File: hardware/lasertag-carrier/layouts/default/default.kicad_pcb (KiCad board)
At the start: 2 copper layers, 100 x 80 mm, 39 parts, among them J0 Power in 2P, J1 S3-Matrix L, J12 Ext button, J13 Touch hdr, J14 Activity LED, J2 S3-Matrix R, J3 MAX98357A, J4 Speaker, J5 microSD, J6 IR RX, J7 IR LED, J8 WS2812 out, J9 OLED I2C, Q1 2N2222A, SW1 SW_PUSH_6mm, SW2 PWR switch

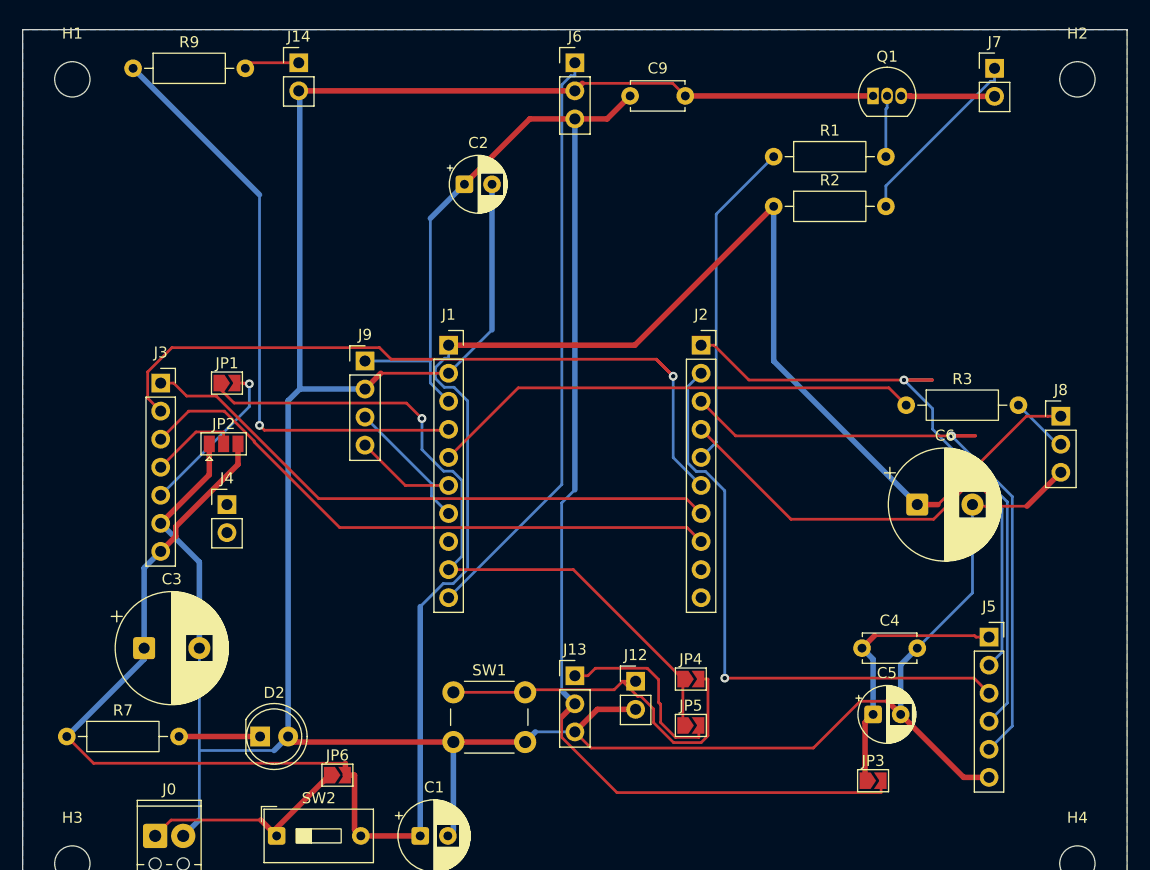
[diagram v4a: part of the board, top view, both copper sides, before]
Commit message: Silk fixes: move edge-clipped refdes inboard, add 5V IN +/- labels
- H1/H2/J6/J14 reference text was clipped by the top board edge; moved below
  each part (silk_edge_clearance 4 -> 0)
- added "5V IN" and +/- polarity marks above J0 (pad 1 = +5V, pad 2 = GND)

Remaining DRC: jumper mask apertures (by design) and 5 track_dangling
warnings that are actually redundant parallel F.Cu/B.Cu segments from the
autorouter -- an independent endpoint-connectivity check confirms both ends
of each are connected (0 unconnected items). Edit > Cleanup Tracks & Vias in
the KiCad GUI removes them if desired.

Co-Authored-By: Claude Opus 4.8 <noreply@anthropic.com>
Claude-Session: https://claude.ai/code/session_01TutNLcDSScdeeVSbjpyg8j
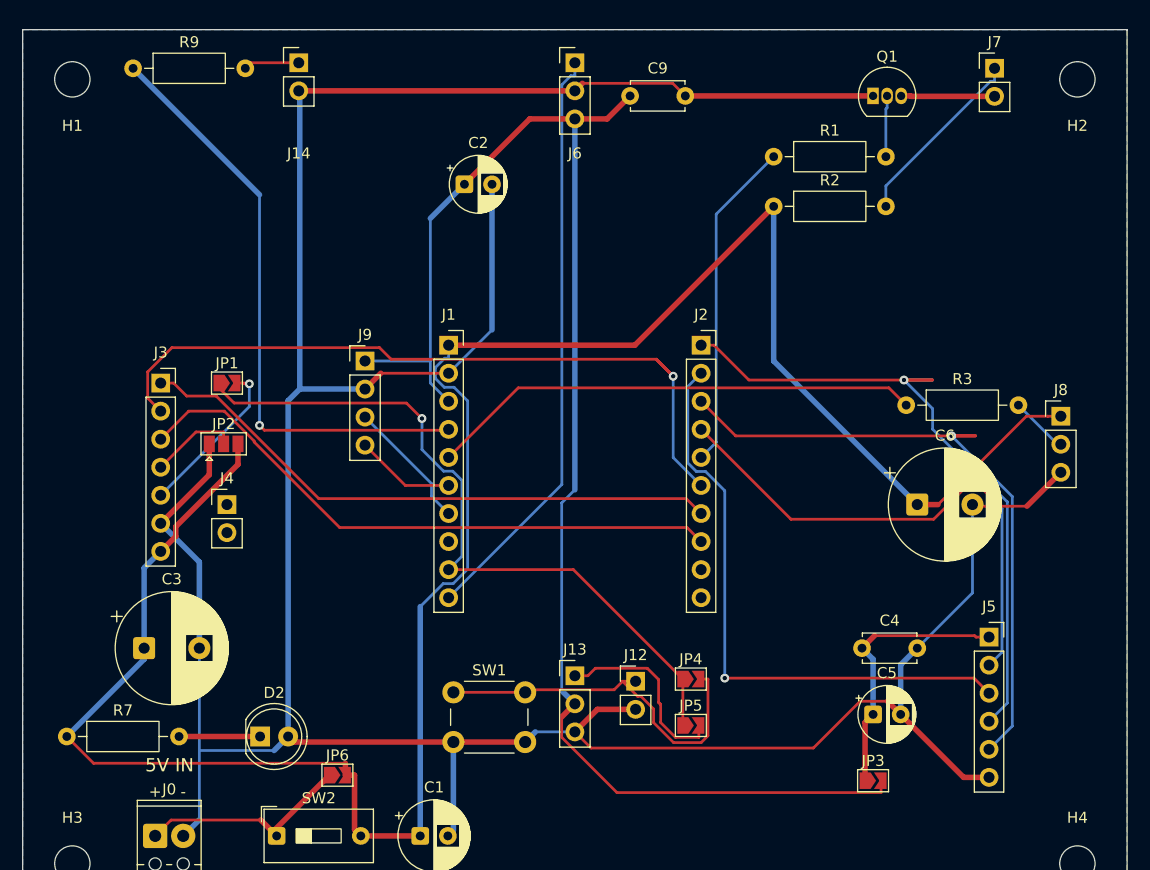
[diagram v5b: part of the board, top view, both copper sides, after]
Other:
- board text added: "+"
- board text added: "-"
- board text added: "5V IN"
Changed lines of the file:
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@@
 		(tags "mountinghole M3")
 		(property "Reference" "H1"
-			(at 0 -4.15 0)
+			(at 0 4.2 0)
 			(layer "F.SilkS")
 			(effects
@@
 		(tags "mountinghole M3")
 		(property "Reference" "H2"
-			(at 0 -4.15 0)
+			(at 0 4.2 0)
 			(layer "F.SilkS")
 			(effects
@@
 		(at 150 63)
 		(property "Reference" "J6"
-			(at 0 -2.38 0)
+			(at 0 8.2 0)
 			(layer "F.SilkS")
 			(effects
@@
 		(at 125 63)
 		(property "Reference" "J14"
-			(at 0 -2.38 0)
+			(at 0 8.2 0)
 			(layer "F.SilkS")
 			(effects
@@
 		(layer "Edge.Cuts")
 	)
+	(gr_text "+"
+		(at 112 129 0)
+		(layer "F.SilkS")
+		(effects
+			(font
+				(size 1 1)
+				(thickness 0.15)
+			)
+		)
+	)
+	(gr_text "-"
+		(at 114.54 129 0)
+		(layer "F.SilkS")
+		(effects
+			(font
+				(size 1 1)
+				(thickness 0.15)
+			)
+		)
+	)
+	(gr_text "5V IN"
+		(at 113.3 126.6 0)
+		(layer "F.SilkS")
+		(effects
+			(font
+				(size 1.2 1.2)
+				(thickness 0.15)
+			)
+		)
+	)
 	(segment

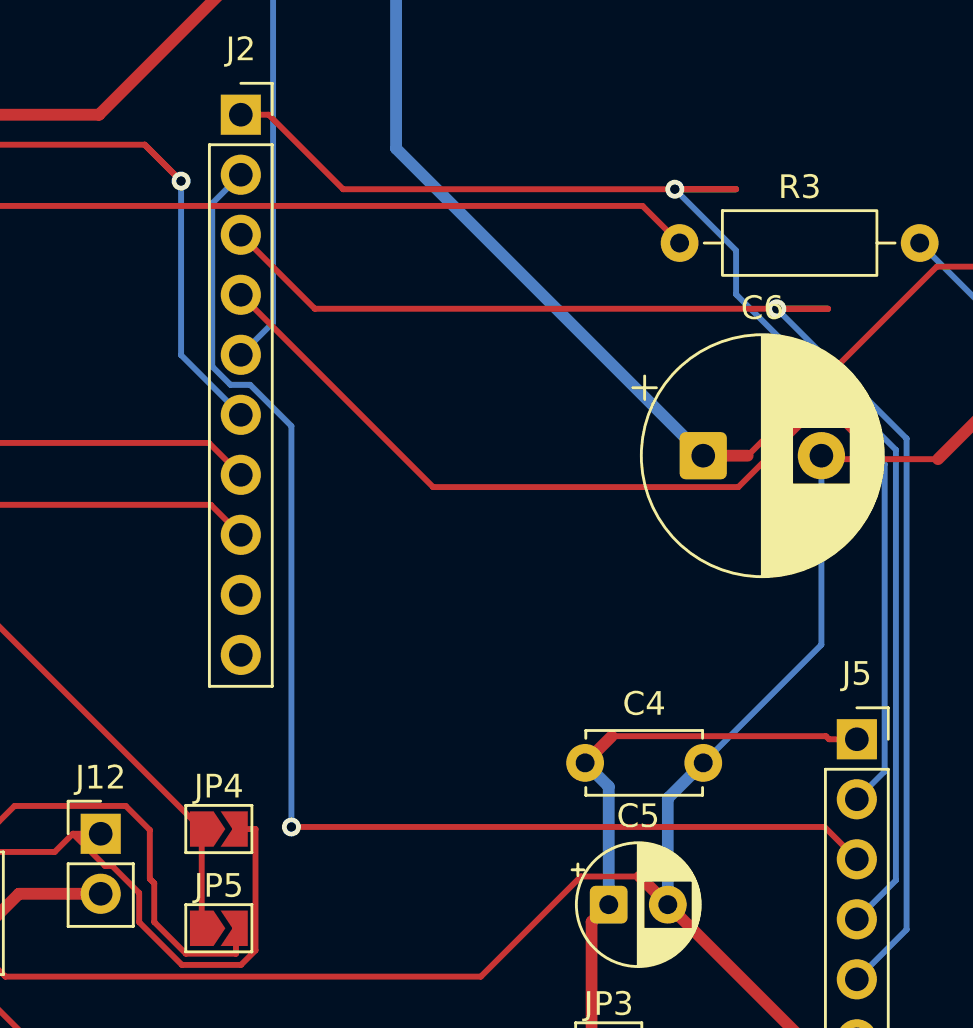
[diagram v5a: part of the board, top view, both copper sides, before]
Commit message: DRC to zero: jumper mask-bridge attr restored, redundant tracks removed
- set allow_soldermask_bridges on all six solder jumpers (JP1-JP6) via
  pcbnew FOOTPRINT.SetAllowSolderMaskBridges(True) -- restores the stock
  KiCad behaviour the atopile footprint patch had stripped; also patched the
  LocalJumper library .kicad_mod files so board and library stay in sync
  (solder_mask_bridge 27 -> 0, lib_footprint_mismatch 0)
- removed 13 redundant autorouter segments: 11 stacked exact duplicates
  (same net + same endpoints, up to 3 copies deep on i2s_bclk) found by
  grouping segments by (net, endpoint-set) and keeping one copy, plus the 2
  remaining parallel loops verified removable by checkpoint + re-DRC
  (track_dangling 5 -> 0); no vias were orphaned

Final DRC: zero violations of any kind, zero unconnected items.

Co-Authored-By: Claude Opus 4.8 <noreply@anthropic.com>
Claude-Session: https://claude.ai/code/session_01TutNLcDSScdeeVSbjpyg8j
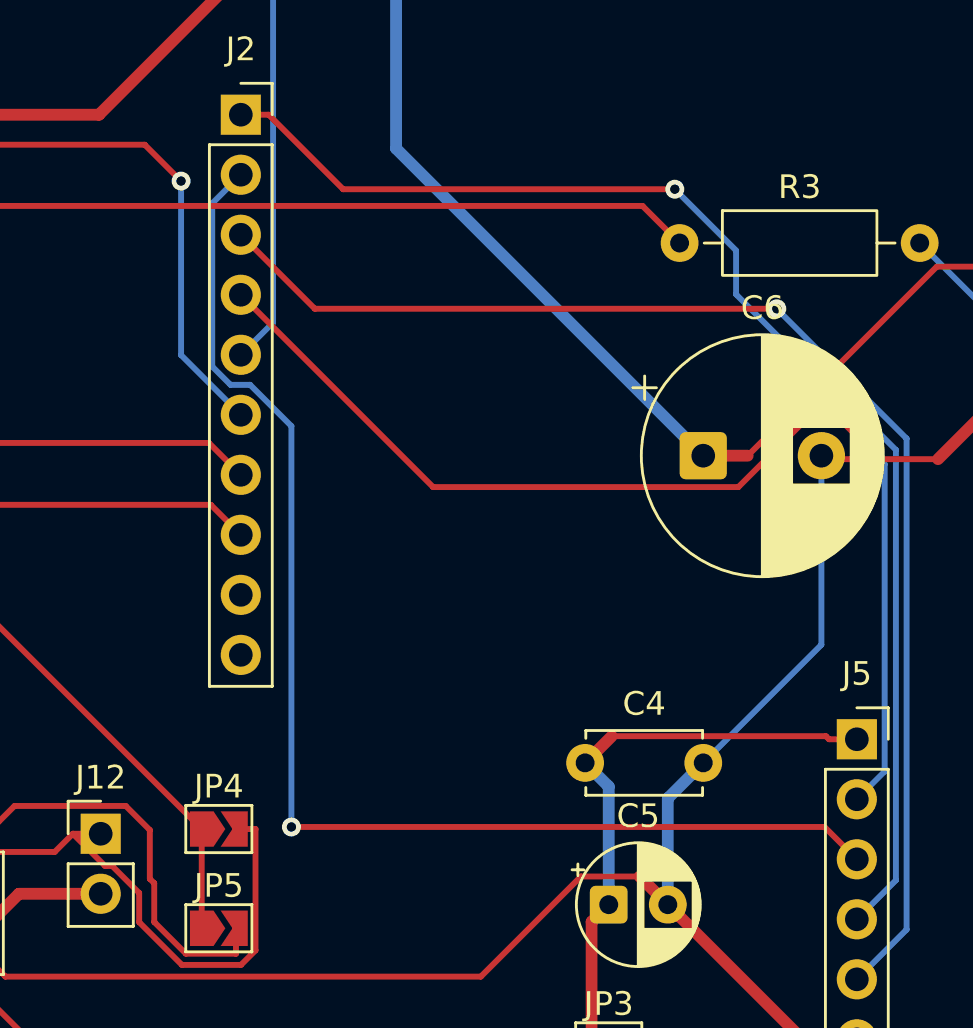
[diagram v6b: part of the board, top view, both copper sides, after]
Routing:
- net sd_sck: track 65.6 -> 55.2 mm
- net i2s_bclk: track 73.2 -> 64.5 mm
- net sd_miso: track 64.2 -> 55.5 mm
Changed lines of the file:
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@@
 			)
 		)
-		(attr exclude_from_pos_files exclude_from_bom)
+		(attr exclude_from_pos_files exclude_from_bom allow_soldermask_bridges)
 		(duplicate_pad_numbers_are_jumpers no)
 		(fp_rect
@@
 			)
 		)
-		(attr exclude_from_pos_files exclude_from_bom)
+		(attr exclude_from_pos_files exclude_from_bom allow_soldermask_bridges)
 		(duplicate_pad_numbers_are_jumpers no)
 		(fp_rect
@@
 			)
 		)
-		(attr exclude_from_pos_files exclude_from_bom)
+		(attr exclude_from_pos_files exclude_from_bom allow_soldermask_bridges)
 		(duplicate_pad_numbers_are_jumpers no)
 		(fp_rect
@@
 			)
 		)
-		(attr exclude_from_pos_files exclude_from_bom)
+		(attr exclude_from_pos_files exclude_from_bom allow_soldermask_bridges)
 		(duplicate_pad_numbers_are_jumpers no)
 		(fp_rect
@@
 		)
 		(zone_connect 1)
-		(attr exclude_from_pos_files exclude_from_bom)
+		(attr exclude_from_pos_files exclude_from_bom allow_soldermask_bridges)
 		(duplicate_pad_numbers_are_jumpers no)
 		(fp_rect
@@
 			)
 		)
-		(attr exclude_from_pos_files exclude_from_bom)
+		(attr exclude_from_pos_files exclude_from_bom allow_soldermask_bridges)
 		(duplicate_pad_numbers_are_jumpers no)
 		(fp_rect
@@
 	)
 	(segment
-		(start 157.7655 121.0932)
-		(end 157.5799 120.9076)
-		(width 0.25)
-		(layer "F.Cu")
-		(net "footprint-b")
-	)
-	(segment
 		(start 157.5799 118.8421)
 		(end 156.5611 117.8233)
@@
 	)
 	(segment
-		(start 182.3908 91.7232)
-		(end 179.7964 91.7232)
-		(width 0.25)
-		(layer "F.Cu")
-		(net "sd_sck")
-	)
-	(segment
-		(start 179.7964 91.7232)
-		(end 182.3908 91.7232)
-		(width 0.25)
-		(layer "F.Cu")
-		(net "sd_sck")
-	)
-	(segment
 		(start 161.43 88.57)
 		(end 162.6067 88.57)
@@
 	)
 	(segment
-		(start 179.7964 91.7232)
-		(end 182.3908 91.7232)
-		(width 0.25)
-		(layer "B.Cu")
-		(net "sd_sck")
-	)
-	(segment
 		(start 189.1537 102.7553)
 		(end 185.96 99.5616)
@@
 	)
 	(segment
-		(start 182.3908 91.7232)
-		(end 179.7964 91.7232)
-		(width 0.25)
-		(layer "B.Cu")
-		(net "sd_sck")
-	)
-	(segment
-		(start 184.1132 96.7816)
-		(end 186.2823 96.7816)
-		(width 0.25)
-		(layer "F.Cu")
-		(net "sd_miso")
-	)
-	(segment
 		(start 164.5616 96.7816)
 		(end 161.43 93.65)
@@
 		(net "sd_miso")
 	)
-	(segment
-		(start 186.2823 96.7816)
-		(end 184.1132 96.7816)
-		(width 0.25)
-		(layer "F.Cu")
-		(net "sd_miso")
-	)
 	(via
 		(at 184.1132 96.7816)
@@
 	)
 	(segment
-		(start 184.1132 96.7816)
-		(end 186.2823 96.7816)
-		(width 0.25)
-		(layer "B.Cu")
-		(net "sd_miso")
-	)
-	(segment
 		(start 189.6054 123.0546)
 		(end 189.6054 102.2738)
@@
 	)
 	(segment
-		(start 186.2823 96.7816)
-		(end 184.1132 96.7816)
-		(width 0.25)
-		(layer "B.Cu")
-		(net "sd_miso")
-	)
-	(segment
 		(start 187.5 125.16)
 		(end 189.6054 123.0546)
@@
 	)
 	(segment
-		(start 157.3632 89.8399)
-		(end 158.9019 91.3786)
-		(width 0.25)
-		(layer "F.Cu")
-		(net "i2s_bclk")
-	)
-	(segment
 		(start 133.3605 89.8399)
 		(end 157.3632 89.8399)
@@
 	)
 	(segment
-		(start 157.3632 89.8399)
-		(end 158.9019 91.3786)
-		(width 0.25)
-		(layer "F.Cu")
-		(net "i2s_bclk")
-	)
-	(segment
 		(start 113.5173 88.7909)
 		(end 132.3115 88.7909)
@@
 	)
 	(segment
-		(start 157.3632 89.8399)
-		(end 158.9019 91.3786)
-		(width 0.25)
-		(layer "B.Cu")
-		(net "i2s_bclk")
-	)
-	(segment
 		(start 158.9019 98.7419)
 		(end 161.43 101.27)
@@
 		(width 0.25)
 		(layer "B.Cu")
-		(net "i2s_bclk")
-	)
-	(segment
-		(start 158.9019 91.3786)
-		(end 157.3632 89.8399)
-		(width 0.25)
-		(layer "B.Cu")
